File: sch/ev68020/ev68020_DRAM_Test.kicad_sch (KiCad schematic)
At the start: 21 parts, among them U10 HC138

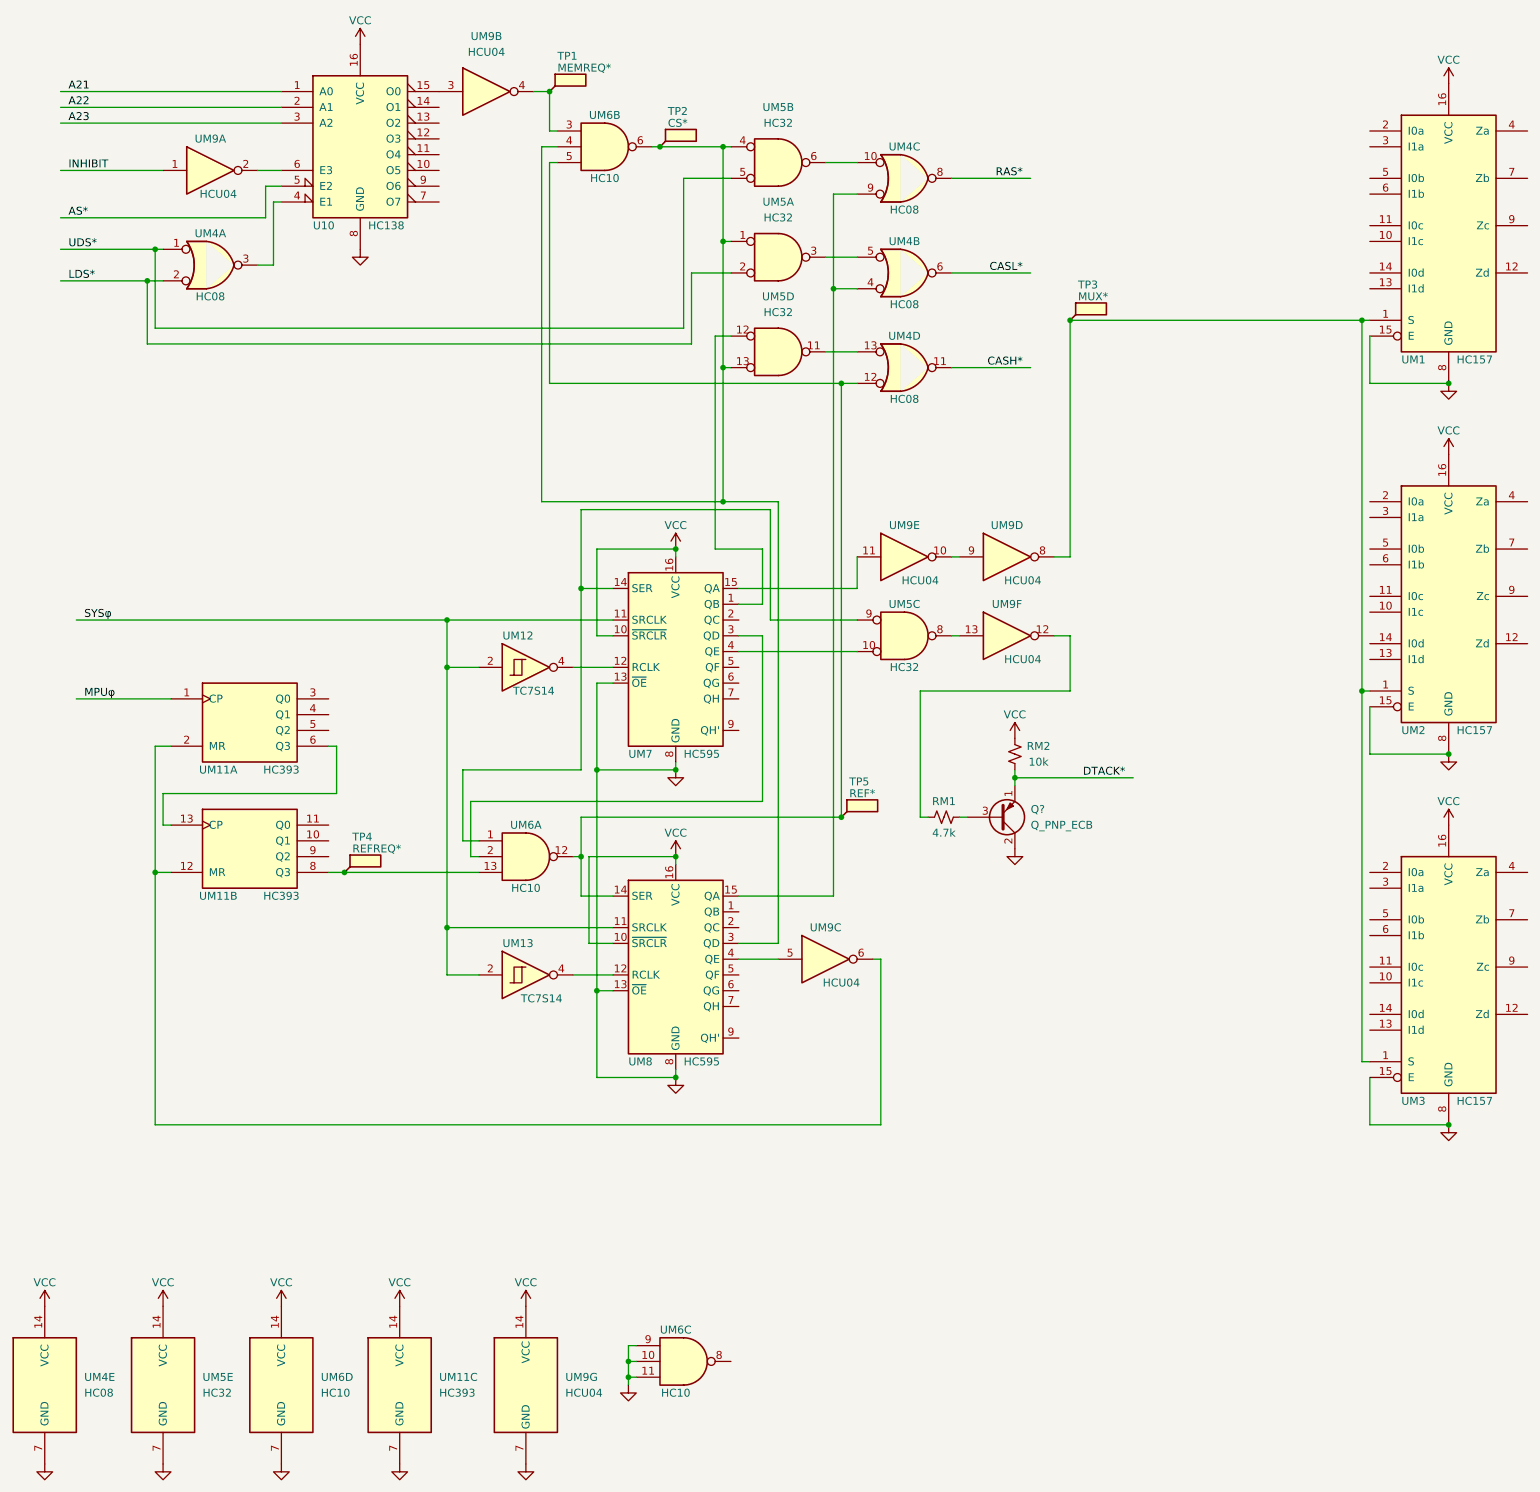
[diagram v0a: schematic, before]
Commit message: minimal fix: change wire attributes
change RAS/CASH/CASL
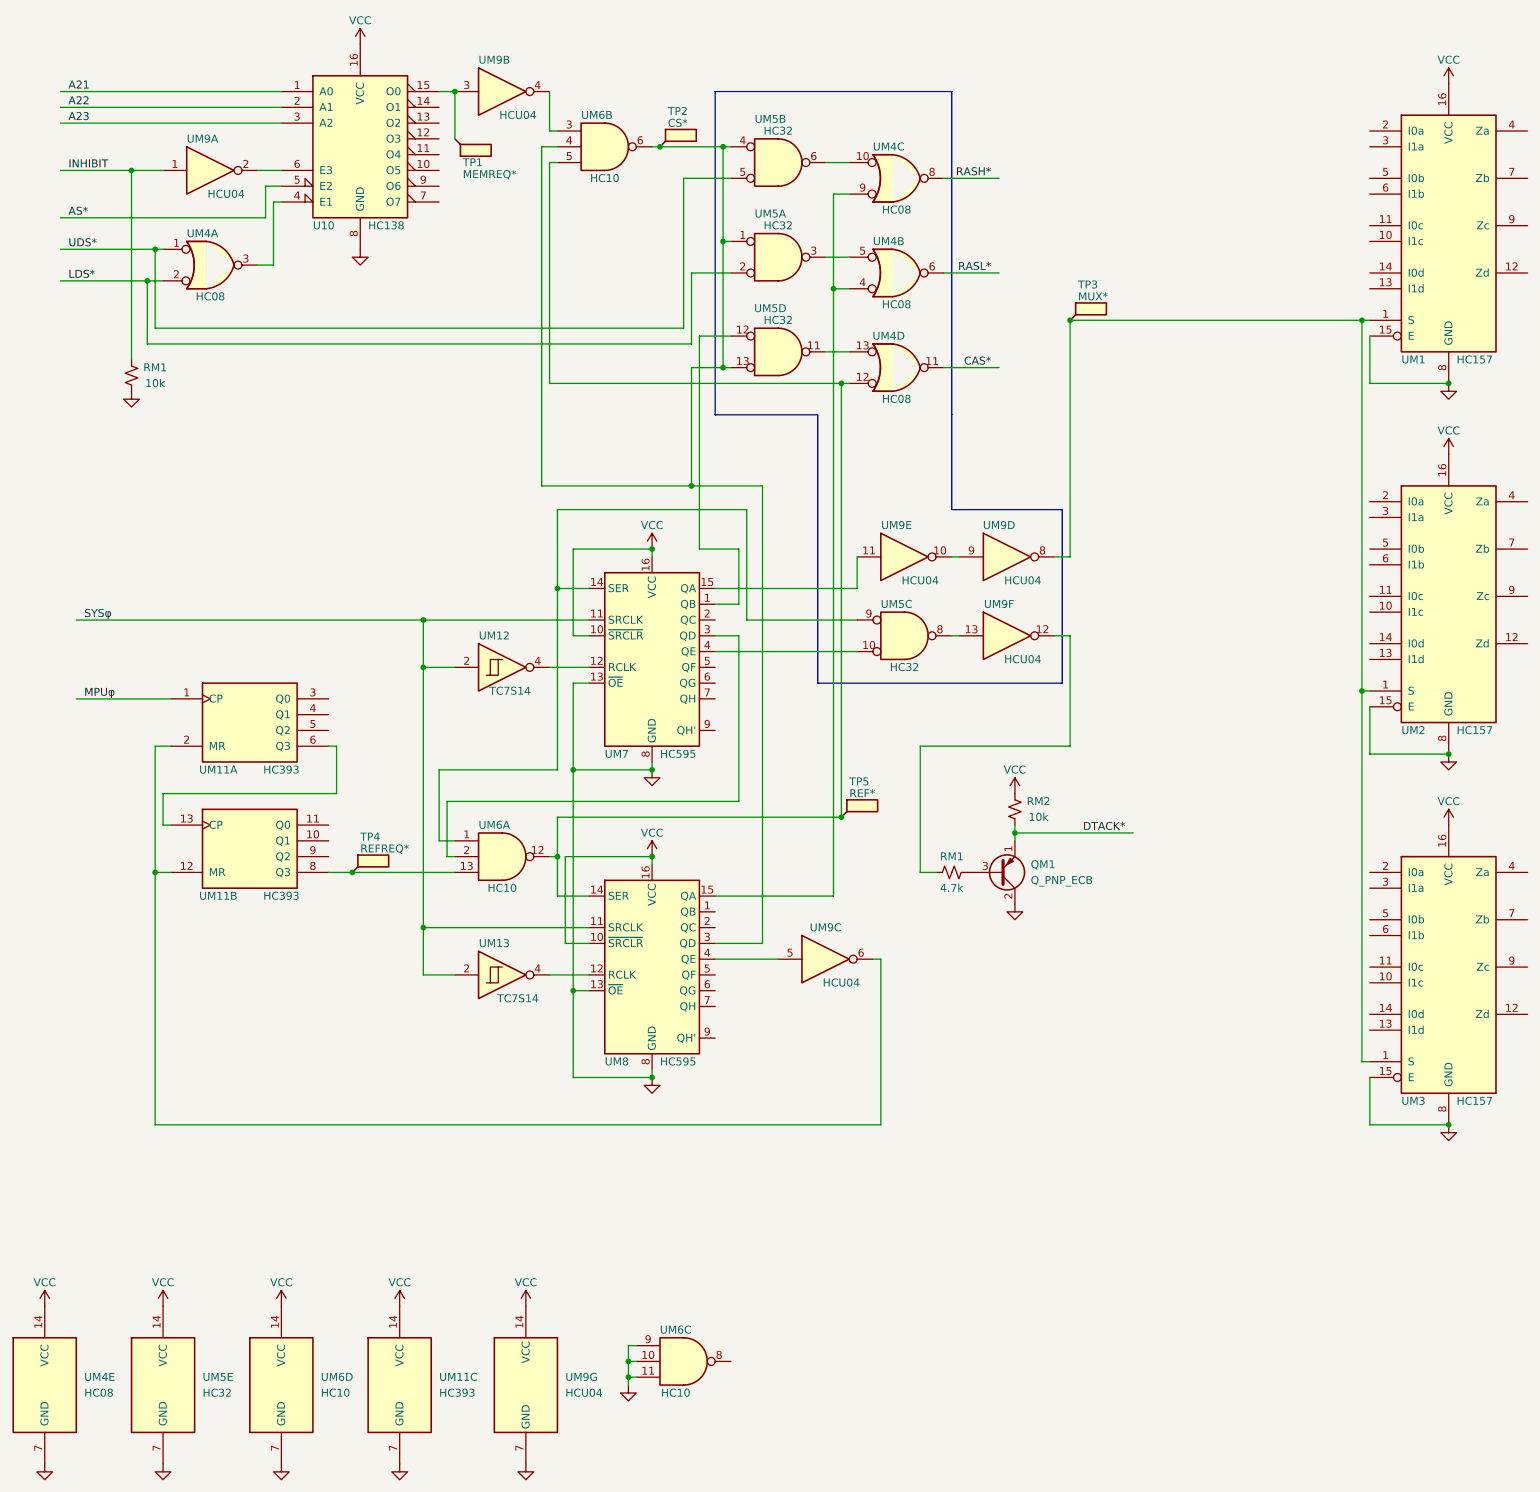
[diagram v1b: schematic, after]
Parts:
- added RM1: 10k, symbol Device:R_Small_US
- gave numbers to parts that had none: 1
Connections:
- net GND: now also RM1.1
- net INHIBIT: now also RM1.2
- net at U10.15 (O0), UM9.3: now also TP1.1
- net at UM6.3, UM9.4: no longer TP1.1
- net CASH* renamed CAS*
- net CASL* renamed RASL*
- net RAS* renamed RASH*
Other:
- moved on the sheet: QM1, RM1, RM2, TP1, TP4, UM12, UM13, UM4B, UM4C, UM4D, UM6A, UM7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
